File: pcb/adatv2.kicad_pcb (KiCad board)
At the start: 2 copper layers, 206 parts, among them J101 TO_IO, J102 TO_DISP_INPUT, J103 TO_DISP_OUTPUT, J104 USB_C_Receptacle_USB2.0_14P, J108 FPGA_JTAG, J202 PLR237, J203 PLT237, J204 PLT237, J205 TO_MAIN, J206 PLR237, J207 PLT237, J208 PLT237, J301 TO_MAIN, U101 10M02SCE144, U107 USB3300-EZK, U108 STM32F427VGTx, U201 AMS1117-3.3, U301 HT1635D, Y103 ECS-TXO-3225MV-122.8-TR

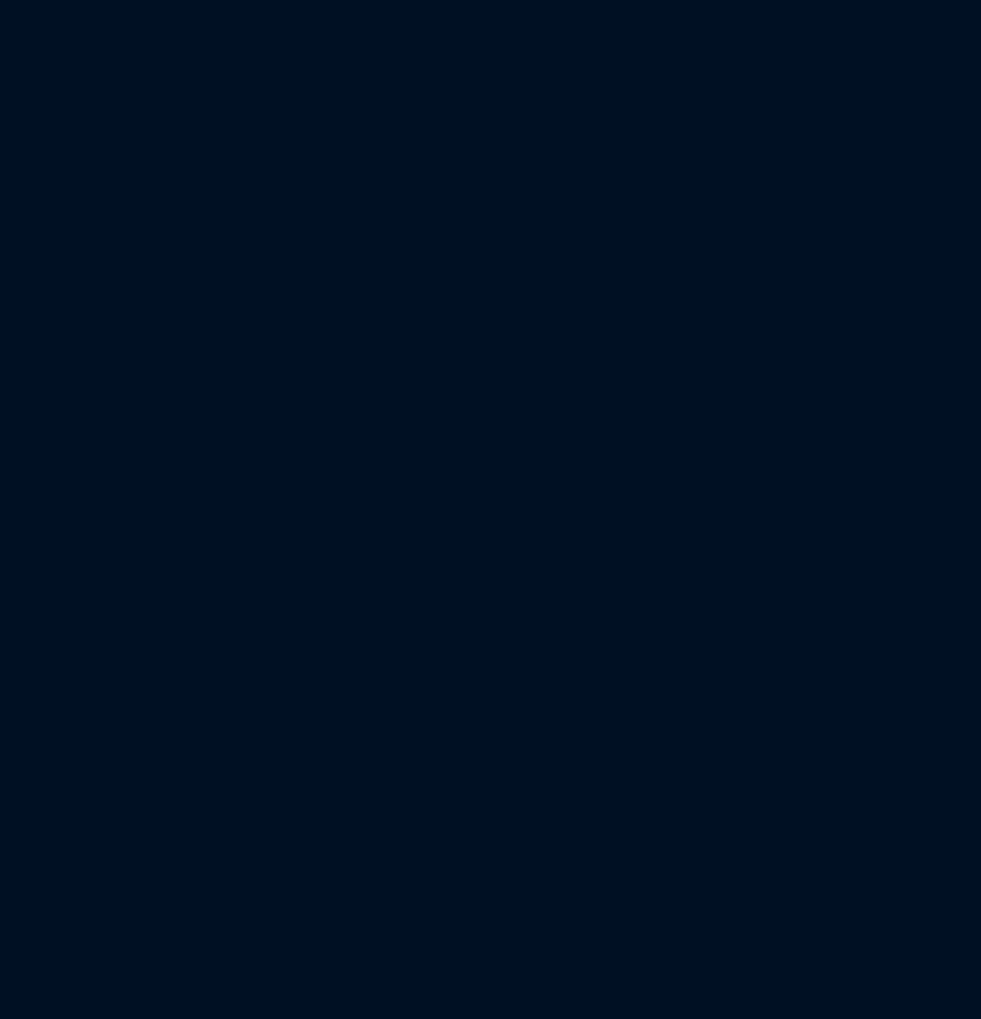
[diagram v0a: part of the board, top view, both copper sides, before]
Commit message: Finish assigning footprints to project
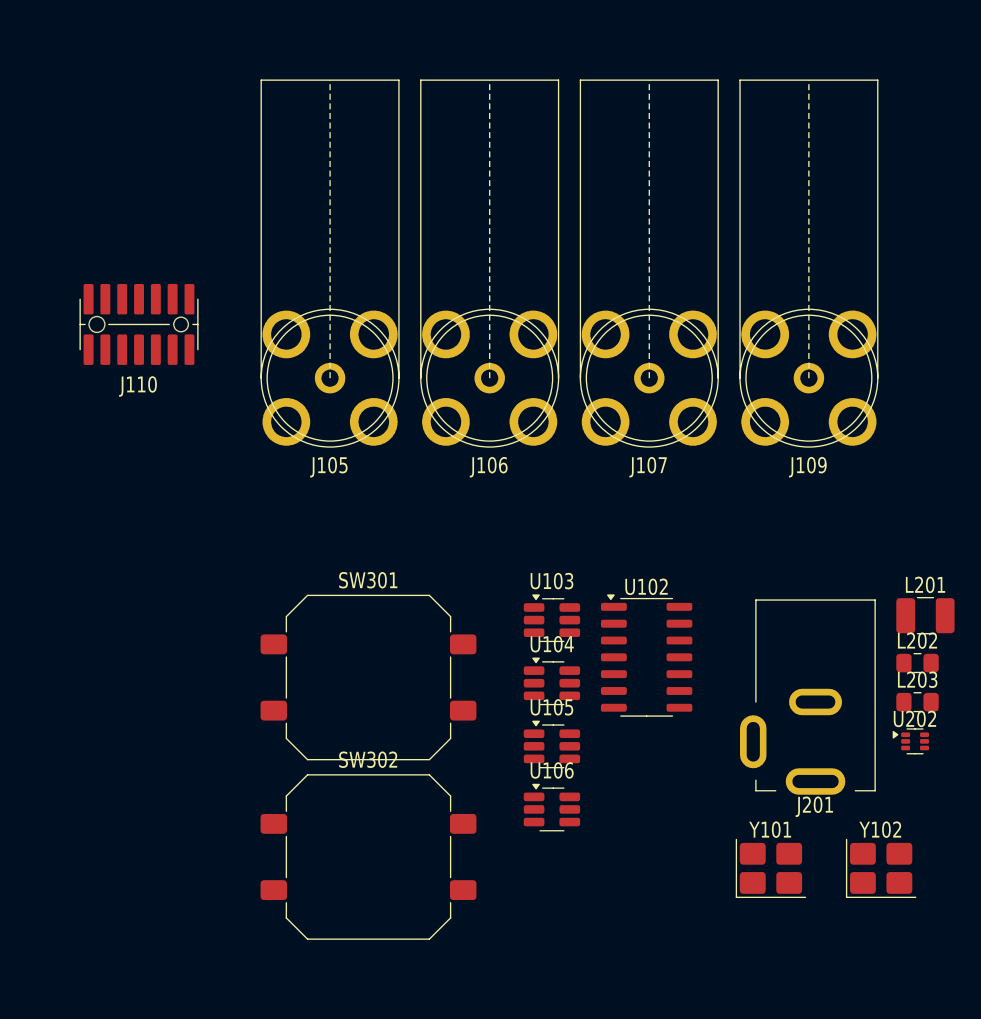
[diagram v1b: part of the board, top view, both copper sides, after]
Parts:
- added J105: WORD_CLK_1, adatv2:BNC_dosinconn_DOSIN-801-0051, F.Cu at (229.3, 88.9)
- added J106: WORD_CLK_2, adatv2:BNC_dosinconn_DOSIN-801-0051, F.Cu at (241.4, 88.9)
- added J107: WORD_CLK_3, adatv2:BNC_dosinconn_DOSIN-801-0051, F.Cu at (253.4, 88.9)
- added J109: FPGA_JTAG, adatv2:BNC_dosinconn_DOSIN-801-0051, F.Cu at (265.5, 88.9)
- added J110: STDC14_SWD, adatv2:Samtec-FTSH-107-01-L-DV-K, F.Cu at (214.9, 84.8)
- added J201: 9-15V DC, adatv2:CUI PJ-002A, F.Cu at (266.0, 112.8)
- added L201: 3.3u, Inductor_SMD:L_1210_3225Metric_Pad1.42x2.65mm_HandSolder, F.Cu at (274.3, 106.8)
- added L202: 47u, Inductor_SMD:L_0805_2012Metric_Pad1.15x1.40mm_HandSolder, F.Cu at (273.7, 110.4)
- added L203: 47u, Inductor_SMD:L_0805_2012Metric_Pad1.15x1.40mm_HandSolder, F.Cu at (273.7, 113.3)
- added SW301: SAMPLE RATE, Button_Switch_SMD:SW_Push_1P1T_NO_CK_PTS125Sx43SMTR, F.Cu at (232.2, 111.5)
- added SW302: LOOPBACK, Button_Switch_SMD:SW_Push_1P1T_NO_CK_PTS125Sx43SMTR, F.Cu at (232.2, 125.0)
- added U102: 74HC14, Package_SO:SOIC-14_3.9x8.7mm_P1.27mm, F.Cu at (253.2, 110.0)
- added U103: 74LVC2G17, Package_TO_SOT_SMD:SOT-23-6_Handsoldering, F.Cu at (246.1, 107.2)
- added U104: 74LVC2G17, Package_TO_SOT_SMD:SOT-23-6_Handsoldering, F.Cu at (246.1, 111.9)
- added U105: 74LVC2G17, Package_TO_SOT_SMD:SOT-23-6_Handsoldering, F.Cu at (246.1, 116.7)
- added U106: 74LVC2G17, Package_TO_SOT_SMD:SOT-23-6_Handsoldering, F.Cu at (246.1, 121.5)
- added U202: TPS56124x, Package_TO_SOT_SMD:SOT-563, F.Cu at (273.5, 116.3)
- added Y101: 24.000MHz, Oscillator:Oscillator_SMD_Abracon_ASE-4Pin_3.2x2.5mm_HandSoldering, F.Cu at (262.6, 125.9)
- added Y102: 11.2896MHz, Oscillator:Oscillator_SMD_Abracon_ASE-4Pin_3.2x2.5mm_HandSoldering, F.Cu at (270.9, 125.9)
- J108: value FPGA_JTAG -> WORD_CLK_4
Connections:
- J108 pad 1: FPGA_TCK -> /IO main/WORD_CLK_4_75_OHM
- J108 pad 10: GND -> (no net)
- J108 pad 3: FPGA_TDO -> (no net)
- J108 pad 4: +3.3V -> (no net)
- J108 pad 5: FPGA_TMS -> (no net)
- J108 pad 6: unconnected-(J108-Pin_6-Pad6) -> (no net)
- J108 pad 7: unconnected-(J108-Pin_7-Pad7) -> (no net)
- J108 pad 8: unconnected-(J108-Pin_8-Pad8) -> (no net)
- J108 pad 9: FPGA_TDI -> (no net)

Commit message: Finish drawing IO/Supply board
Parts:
- removed U108: STM32F427VGTx, Package_QFP:LQFP-100_14x14mm_P0.5mm
- added C149: 10p, Capacitor_SMD:C_0805_2012Metric_Pad1.18x1.45mm_HandSolder, F.Cu at (111.9, 115.0)
- added C150: 1u, Capacitor_SMD:C_0805_2012Metric_Pad1.18x1.45mm_HandSolder, F.Cu at (46.4, 125.3)
- added D108: 3V, Diode_SMD:D_SOD-123, F.Cu at (51.8, 124.9)
- added R132: 1k, Resistor_SMD:R_0805_2012Metric_Pad1.20x1.40mm_HandSolder, F.Cu at (75.1, 105.7)
- added TP201: +12V_IO, TestPoint:TestPoint_Pad_D2.5mm, F.Cu at (311.9, 34.8)
- added TP202: +5V_IO, TestPoint:TestPoint_Pad_D2.5mm, F.Cu at (305.5, 34.8)
- added TP203: +3.3V_IO, TestPoint:TestPoint_Pad_D2.5mm, F.Cu at (299.2, 34.8)
- C128, C205, C206, C208: footprint Capacitor_SMD:C_0805_2012Metric_Pad1.18x1.45mm_HandSolder -> Capacitor_SMD:C_1206_3216Metric_Pad1.33x1.80mm_HandSolder
- C138: value 100n -> 4.7u
- C140: value 4.7u -> 2.2u
- C142: value 2.2u -> 15pF
- C143: value C_{load} -> 15pF
- C144: value C_{load} -> 10u; footprint Capacitor_SMD:C_0805_2012Metric_Pad1.18x1.45mm_HandSolder -> Capacitor_SMD:C_1206_3216Metric_Pad1.33x1.80mm_HandSolder
- C146: value 10p -> 10u; footprint Capacitor_SMD:C_0805_2012Metric_Pad1.18x1.45mm_HandSolder -> Capacitor_SMD:C_1206_3216Metric_Pad1.33x1.80mm_HandSolder
- C147: value 10p -> 100n
- J104: value USB_C_Receptacle_USB2.0_14P -> WORD_CLK_1; footprint Connector_USB:USB_C_Receptacle_GCT_USB4105-xx-A_16P_TopMnt_Horizontal -> adatv2:BNC_dosinconn_DOSIN-801-0051
- J105: value WORD_CLK_1 -> USB_C_Receptacle_USB2.0_14P; footprint adatv2:BNC_dosinconn_DOSIN-801-0051 -> Connector_USB:USB_C_Receptacle_GCT_USB4105-xx-A_16P_TopMnt_Horizontal
- J108: footprint Connector_IDC:IDC-Header_2x05_P2.54mm_Vertical -> adatv2:BNC_dosinconn_DOSIN-801-0051
- J109: footprint adatv2:BNC_dosinconn_DOSIN-801-0051 -> Connector_IDC:IDC-Header_2x05_P2.54mm_Vertical
- R121: value 1M -> 150
- R122: value 150 -> 5.1k
- R124: value 5.1k -> 150
- R131: value 150 -> 1k
- U102: value 74HC14 -> 74LVC2G17; footprint Package_SO:SOIC-14_3.9x8.7mm_P1.27mm -> Package_TO_SOT_SMD:SOT-23-6_Handsoldering
- U106: value 74LVC2G17 -> USB3300-EZK; footprint Package_TO_SOT_SMD:SOT-23-6_Handsoldering -> Package_DFN_QFN:QFN-32-1EP_5x5mm_P0.5mm_EP3.45x3.45mm
- U107: value USB3300-EZK -> STM32F427VGTx; footprint Package_DFN_QFN:QFN-32-1EP_5x5mm_P0.5mm_EP3.45x3.45mm -> Package_QFP:LQFP-100_14x14mm_P0.5mm
- Y102: value 11.2896MHz -> OT2EL89CJI-111YLC-11.2896M
- moved H204 282.1 mm to (324.5, 35.0), turned to 180 degrees
- moved BAR308 268.2 mm to (332.8, 137.8)
- moved BAR307 267.0 mm to (320.9, 137.8)
- moved BAR306 265.9 mm to (308.9, 137.8)
- moved BAR305 264.8 mm to (297.0, 137.8)
- moved BAR304 263.7 mm to (285.1, 137.8)
- moved BAR303 262.6 mm to (273.2, 137.8)
- moved BAR302 261.4 mm to (261.3, 137.8)
- moved H201 261.4 mm to (324.5, 79.0), turned to 180 degrees
- moved BAR301 260.3 mm to (249.4, 137.8)
- moved J205 244.9 mm to (323.8, 68.3), turned to 180 degrees
- moved J301 230.4 mm to (278.8, 196.0)
- moved C301 230.4 mm to (314.9, 210.9)
- moved C302 230.4 mm to (314.9, 213.9)
- moved C303 230.4 mm to (314.9, 216.9)
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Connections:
- net FPGA_JTAGEN renamed Net-(U101B-JTAGEN)
- net Net-(D201-A) renamed /IO board/POWER_IN
- net Net-(U202-SW) renamed /IO board/SMPS_POWER_OUT
- C137 pad 1: +3.3V -> MCU_RESET
- C138 pad 1: MCU_RESET -> Net-(C138-Pad1)
- C139 pad 1: Net-(C139-Pad1) -> Net-(U106-VDDA1.8)
- C140 pad 1: Net-(U107-VDDA1.8) -> Net-(U107-VCAP_1)
- C141 pad 1: Net-(U108-VCAP_1) -> Net-(U107-VCAP_2)
- C142 pad 1: Net-(U108-VCAP_2) -> MCU_XTAL2
- C143 pad 1: MCU_XTAL2 -> MCU_XTAL1
- C144 pad 1: MCU_XTAL1 -> +3.3V
- C146 pad 1: /FPGA and clock generators/CLK_48000 -> +3.3V
- C147 pad 1: Net-(C147-Pad1) -> +3.3V
- C148 pad 1: Net-(C148-Pad1) -> /FPGA and clock generators/CLK_44100
- C210 pad 1: +3.3V_IO -> Net-(J202-VCC)
- C213 pad 1: +3.3V_IO -> Net-(J206-VCC)
- H201 pad 1: GND -> GND_IO
- H202 pad 1: GND -> GND_IO
- H203 pad 1: GND -> GND_IO
- H204 pad 1: GND -> GND_IO
- H301 pad 1: GND -> DISPLAY_GND
- H302 pad 1: GND -> DISPLAY_GND
- J101 pad 10: GND_IO -> GND
- J101 pad 12: GND_IO -> GND
- J101 pad 14: GND_IO -> GND
- J101 pad 16: GND_IO -> GND
- J101 pad 18: GND_IO -> GND
- J101 pad 20: GND_IO -> GND
- J101 pad 7: GND_IO -> GND
- J101 pad 8: GND_IO -> GND
- J202 pad 4: (no net) -> unconnected-(J202-NC-Pad4)
- J202 pad 5: (no net) -> unconnected-(J202-NC-Pad5)
- J203 pad 4: (no net) -> unconnected-(J203-NC-Pad4)
- J203 pad 5: (no net) -> unconnected-(J203-NC-Pad5)
- J204 pad 4: (no net) -> unconnected-(J204-NC-Pad4)
- J204 pad 5: (no net) -> unconnected-(J204-NC-Pad5)
- J206 pad 4: (no net) -> unconnected-(J206-NC-Pad4)
- J206 pad 5: (no net) -> unconnected-(J206-NC-Pad5)
- J207 pad 4: (no net) -> unconnected-(J207-NC-Pad4)
- J207 pad 5: (no net) -> unconnected-(J207-NC-Pad5)
- J208 pad 4: (no net) -> unconnected-(J208-NC-Pad4)
- J208 pad 5: (no net) -> unconnected-(J208-NC-Pad5)
- L202 pad 1: Net-(J202-VCC) -> +3.3V_IO
- L202 pad 2: +3.3V_IO -> Net-(J202-VCC)
- L203 pad 1: Net-(J206-VCC) -> +3.3V_IO
- L203 pad 2: +3.3V_IO -> Net-(J206-VCC)
- R101 pad 1: Net-(U107-VBUS) -> Net-(U106-VBUS)
- R102 pad 2: Net-(U107-RBIAS) -> Net-(U106-RBIAS)
- R103 pad 1: Net-(U108-PB14) -> Net-(U107-PB14)
- R104 pad 1: Net-(U108-PB15) -> Net-(U107-PB15)
- R105 pad 1: Net-(U108-PC11) -> Net-(U107-PC11)
- R106 pad 1: Net-(U108-PC12) -> Net-(U107-PC12)
- R114 pad 2: +5V -> Net-(D108-K)
- R115 pad 2: +5V -> Net-(D108-K)
- R121 pad 1: Net-(C147-Pad1) -> Net-(R121-Pad1)
- R121 pad 2: Net-(C148-Pad1) -> /IO main/WORD_CLK_1_75_OHM
- R122 pad 1: Net-(R122-Pad1) -> Net-(J105-CC1)
- R122 pad 2: /IO main/WORD_CLK_1_75_OHM -> GND
- R123 pad 1: Net-(J104-CC1) -> Net-(J105-CC2)
- R124 pad 1: Net-(J104-CC2) -> Net-(R124-Pad1)
- R124 pad 2: GND -> /IO main/WORD_CLK_1_75_OHM
- R125 pad 2: /IO main/WORD_CLK_1_75_OHM -> /IO main/WORD_CLK_2_75_OHM
- R127 pad 2: /IO main/WORD_CLK_2_75_OHM -> /IO main/WORD_CLK_3_75_OHM
- R129 pad 2: /IO main/WORD_CLK_3_75_OHM -> /IO main/WORD_CLK_4_75_OHM
- R131 pad 1: Net-(R131-Pad1) -> +5V
- R131 pad 2: /IO main/WORD_CLK_4_75_OHM -> Net-(D108-K)
- U102 pad 1: Net-(C147-Pad1) -> WORD_CLK
- U102 pad 2: Net-(C148-Pad1) -> GND
- U102 pad 3: Net-(C148-Pad1) -> WORD_CLK
- U102 pad 4: /FPGA and clock generators/CLK_44100 -> Net-(R124-Pad1)
- U102 pad 6: unconnected-(U102-Pad6) -> Net-(R121-Pad1)
- U103 pad 4: Net-(R125-Pad1) -> Net-(R126-Pad1)
- U103 pad 6: Net-(R122-Pad1) -> Net-(R125-Pad1)
- U104 pad 4: Net-(R127-Pad1) -> Net-(R128-Pad1)
- U104 pad 6: Net-(R126-Pad1) -> Net-(R127-Pad1)
- U105 pad 4: Net-(R129-Pad1) -> Net-(R130-Pad1)
- U105 pad 6: Net-(R128-Pad1) -> Net-(R129-Pad1)
- U106 pad 1: WORD_CLK -> GND
- U106 pad 3: WORD_CLK -> unconnected-(U106-CPEN-Pad3)
- U106 pad 4: Net-(R131-Pad1) -> Net-(U106-VBUS)
- U106 pad 5: +3.3V -> unconnected-(U106-ID-Pad5)
- U106 pad 6: Net-(R130-Pad1) -> +3.3V
- U107 pad 1: GND -> MCU_DEBUG2
- U107 pad 10: unconnected-(U107-EXTVBUS-Pad10) -> GND
- U107 pad 11: /MCU and USB/ULPI_NXT -> +3.3V
- U107 pad 12: /MCU and USB/ULPI_DIR -> MCU_XTAL1
- U107 pad 13: /MCU and USB/ULPI_STP -> MCU_XTAL2
- U107 pad 14: /MCU and USB/ULPI_CLK -> MCU_RESET
- U107 pad 15: Net-(C139-Pad1) -> /MCU and USB/ULPI_STP
- U107 pad 16: +3.3V -> unconnected-(U107-PC1-Pad16)
- U107 pad 17: /MCU and USB/ULPI_D7 -> /MCU and USB/ULPI_DIR
- U107 pad 18: /MCU and USB/ULPI_D6 -> /MCU and USB/ULPI_NXT
- U107 pad 19: /MCU and USB/ULPI_D5 -> +3.3V
- U107 pad 2: GND -> MCU_DEBUG3
- U107 pad 20: /MCU and USB/ULPI_D4 -> GND
- U107 pad 21: /MCU and USB/ULPI_D3 -> +3.3V
- U107 pad 22: /MCU and USB/ULPI_D2 -> +3.3V
- U107 pad 23: /MCU and USB/ULPI_D1 -> unconnected-(U107-PA0-Pad23)
- U107 pad 24: /MCU and USB/ULPI_D0 -> unconnected-(U107-PA1-Pad24)
- U107 pad 25: +3.3V -> unconnected-(U107-PA2-Pad25)
- U107 pad 26: Net-(C139-Pad1) -> /MCU and USB/ULPI_D0
- U107 pad 27: unconnected-(U107-XO-Pad27) -> GND
- U107 pad 28: /MCU and USB/MCO1 -> +3.3V
- U107 pad 29: Net-(U107-VDDA1.8) -> I2S_CH9-16_LRCLK
- U107 pad 3: unconnected-(U107-CPEN-Pad3) -> ADAT_IN1_USER0
- U107 pad 30: +3.3V -> /MCU and USB/ULPI_CLK
- U107 pad 31: +3.3V -> /MCU and USB/USB_RESET
- U107 pad 32: Net-(U107-RBIAS) -> unconnected-(U107-PA7-Pad32)
- U107 pad 33: GND -> unconnected-(U107-PC4-Pad33)
- U107 pad 4: Net-(U107-VBUS) -> ADAT_IN1_USER1
- U107 pad 5: unconnected-(U107-ID-Pad5) -> ADAT_IN1_USER2
- U107 pad 7: USB_D+ -> unconnected-(U107-PC13-Pad7)
- U107 pad 8: USB_D- -> unconnected-(U107-PC14-Pad8)
- U107 pad 9: GND -> unconnected-(U107-PC15-Pad9)
- Y101 pad 3: GND -> MCU_XTAL1
- Y101 pad 4: MCU_XTAL1 -> GND
- Y102 pad 1: Net-(C147-Pad1) -> +3.3V
- Y102 pad 3: GND -> /FPGA and clock generators/CLK_44100
- Y102 pad 4: Net-(C148-Pad1) -> +3.3V
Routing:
- net +3.3V_IO: track 0.00 -> 228.4 mm, vias 0 -> 7
- net +5V_IO: track 0.00 -> 212.2 mm, vias 0 -> 3
- net +12V_IO: track 0.00 -> 197.0 mm, vias 0 -> 3
- net /IO board/IO_ADAT_IN1: track 0.00 -> 151.2 mm
- net /IO board/IO_ADAT_IN2: track 0.00 -> 112.8 mm
- net /IO board/IO_ADAT_OUT1: track 0.00 -> 88.4 mm
- net /IO board/IO_ADAT_OUT2: track 0.00 -> 65.3 mm
- net /IO board/IO_ADAT_THRU1: track 0.00 -> 58.9 mm
- net /IO board/IO_ADAT_THRU2: track 0.00 -> 46.4 mm
- net /IO board/SMPS_POWER_OUT: track 0.00 -> 14.4 mm
- net /IO board/SMPS_FEEDBACK: track 0.00 -> 8.82 mm
- net Net-(J206-VCC): track 0.00 -> 6.12 mm
- net Net-(J202-VCC): track 0.00 -> 6.09 mm
- net /IO board/POWER_IN: track 0.00 -> 5.29 mm
- net Net-(U202-BST): track 0.00 -> 4.82 mm
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- added copper zone on B.Cu, net GND_IO
- added copper zone on F.Cu, net GND_IO
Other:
- board outline added: 150 x 56 mm
- copper layers 2 -> 4
- board text added: "${REVISION} ${CURRENT_DATE}"
- board text added: "+12V"
- board text added: "+3V"
- board text added: "+5V"
- board text added: "+9 - 15V"
- board text added: "4xADAT Interface - IO/Supply Board Rev: Date:"
- board text added: "ADAT IN"
- board text added: "ADAT OUT"
- board text added: "ADAT THRU"
- board text added: "CH 1-8"
- board text added: "CH 9-16"
- board text added: "DC IN"
- board text added: "TEST POINTS"

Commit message: Draw first version of display board
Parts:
- BAR301, BAR302, BAR303, BAR304, BAR305, BAR306, BAR307, BAR308, BAR309, BAR310, BAR311, BAR312, BAR313, BAR314, BAR315, BAR316: value HDSP-4832_2 -> KYX-B10BRYG-3; footprint Display:HDSP-4832 -> adatv2:LED_10bar; moved to B.Cu
- D301, D302, D303, D304, D305, D306, D307, D308, SW301, SW302: moved to B.Cu
- moved C207 216.0 mm to (40.6, 196.2)
- moved C210 216.0 mm to (62.0, 226.2)
- moved C211 216.0 mm to (101.9, 225.7)
- moved C213 216.0 mm to (77.0, 226.2)
- moved C214 216.0 mm to (116.8, 225.7)
- moved D201 216.0 mm to (34.3, 222.7)
- moved L201 216.0 mm to (54.4, 209.8)
- moved L202 216.0 mm to (65.0, 225.2)
- moved L203 216.0 mm to (80.0, 225.2)
- moved R201 216.0 mm to (47.5, 214.3)
- moved R202 216.0 mm to (42.7, 208.2)
- moved R204 216.0 mm to (106.4, 224.7)
- moved R205 216.0 mm to (146.6, 224.7)
- moved U202 216.0 mm to (45.5, 211.0)
- moved C201 216.0 mm to (39.9, 208.2)
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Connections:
- net Net-(C301-Pad1) renamed /Display board/DISPLAY_VCC
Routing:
- net /Display board/COM0: track 0.00 -> 311.4 mm, vias 0 -> 5
- net /Display board/COM1: track 0.00 -> 265.3 mm, vias 0 -> 5
- net /Display board/COM2: track 0.00 -> 251.2 mm, vias 0 -> 4
- net /Display board/COM3: track 0.00 -> 229.2 mm, vias 0 -> 7
- net /Display board/COM4: track 0.00 -> 219.8 mm, vias 0 -> 8
- net /Display board/COM6: track 0.00 -> 206.6 mm, vias 0 -> 6
- net /Display board/COM5: track 0.00 -> 203.2 mm, vias 0 -> 6
- net /Display board/COM7: track 0.00 -> 182.3 mm, vias 0 -> 6
- net /Display board/LED9: track 0.00 -> 149.6 mm
- net /Display board/LED8: track 0.00 -> 141.9 mm
- net /Display board/LED7: track 0.00 -> 136.5 mm
- net /Display board/LED6: track 0.00 -> 130.2 mm
- net /Display board/LED5: track 0.00 -> 125.6 mm
- net Net-(U301-ROW0): track 0.00 -> 123.4 mm, vias 0 -> 2
- net /Display board/LED4: track 0.00 -> 118.2 mm
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- added copper zone on B.Cu, net DISPLAY_GND
- added copper zone on F.Cu, net DISPLAY_GND
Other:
- board size 150 x 56 mm -> 371.6 x 208.9 mm
- board text added: "${CURRENT_DATE}"
- board text added: "${REVISION}"
- board text added: "4xADAT Interface - Display Board Rev:"
- board text added: "CH1"
- board text added: "CH10"
- board text added: "CH11"
- board text added: "CH12"
- board text added: "CH13"
- board text added: "CH14"
- board text added: "CH15"
- board text added: "CH16"
- board text added: "CH2"
- board text added: "CH3"
- board text added: "CH4"
- board text added: "CH5"
- board text added: "CH6"
- board text added: "CH7"
- board text added: "CH8"
- board text added: "CH9"
- board text added: "Date:"
- board text added: "INPUT"
- board text added: "LEVEL METERS"
- board text removed: "+12V"

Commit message: Small display board layout improvements
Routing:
- net /Display board/DISPLAY_VCC: track 87.1 -> 88.4 mm
- net Net-(U301-ROW8): track 76.2 -> 75.1 mm
- net Net-(U301-ROW9): track 72.2 -> 71.3 mm
- net Net-(U301-ROW7): track 81.2 -> 80.3 mm
- net Net-(U301-ROW6): track 85.3 -> 84.4 mm
- net Net-(U301-ROW5): track 90.0 -> 89.1 mm
- net Net-(U301-ROW4): track 94.2 -> 93.6 mm
- net Net-(U301-ROW0): track 123.4 -> 123.9 mm
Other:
- outline, holes or cut-outs redrawn
- board text added: "TO MAIN BOARD"

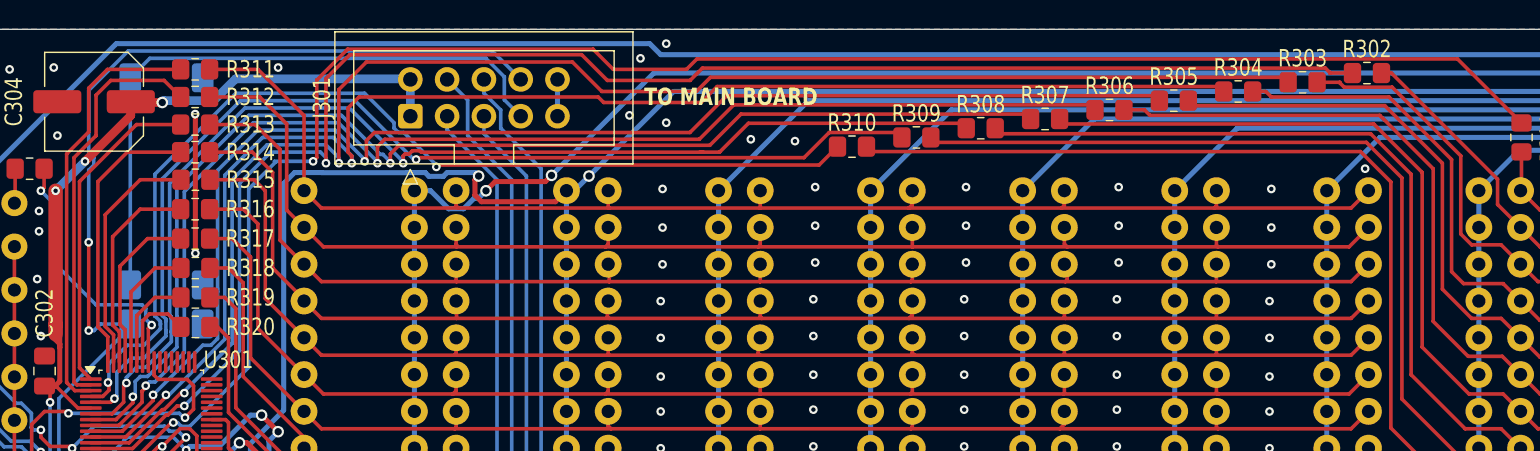
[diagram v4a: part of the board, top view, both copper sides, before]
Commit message: Small display board layout improvements
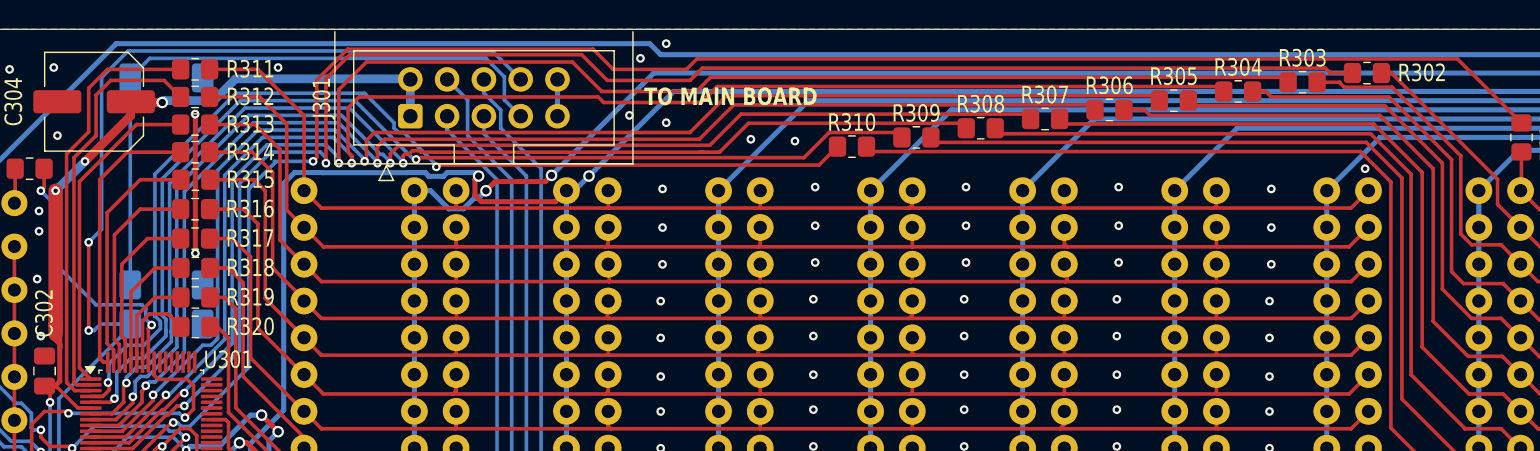
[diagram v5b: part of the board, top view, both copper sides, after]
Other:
- board text added: "STATUS"

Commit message: Add missing CAD models of I/O electronic components
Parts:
- R103, R104, R105, R106: value 1k -> 150
- U101: footprint Package_QFP:EQFP-144-1EP_20x20mm_P0.5mm_EP4x4mm_ThermalVias -> adatv2:EQFP-144-1EP_20x20mm_P0.5mm_EP4x4mm
